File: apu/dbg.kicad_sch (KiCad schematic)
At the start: 12 parts, among them U1 X818336-001, U3 AT25xxx

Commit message: Internal Connectors
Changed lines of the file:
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@@
 	(bus
 		(pts
-			(xy 31.75 71.12) (xy 36.83 71.12)
+			(xy 34.29 71.12) (xy 36.83 71.12)
 		)
 		(stroke
@@
 	(bus
 		(pts
-			(xy 143.51 68.58) (xy 148.59 68.58)
+			(xy 148.59 66.04) (xy 148.59 68.58)
 		)
 		(stroke
@@
 	(bus
 		(pts
-			(xy 125.73 63.5) (xy 130.81 63.5)
-		)
-		(stroke
-			(width 0)
-			(type default)
-		)
-	)
-	(bus
-		(pts
-			(xy 262.89 71.12) (xy 267.97 71.12)
+			(xy 125.73 63.5) (xy 125.73 60.96)
+		)
+		(stroke
+			(width 0)
+			(type default)
+		)
+	)
+	(bus
+		(pts
+			(xy 262.89 71.12) (xy 262.89 68.58)
 		)
 		(stroke
@@
 	(hierarchical_label "{XCGPU_DBG}"
 		(shape bidirectional)
-		(at 31.75 71.12 180)
+		(at 34.29 71.12 180)
 		(effects
 			(font
@@
 	(hierarchical_label "{XCGPU_DBG}"
 		(shape bidirectional)
-		(at 130.81 63.5 0)
+		(at 125.73 60.96 90)
 		(effects
 			(font
@@
 	(hierarchical_label "XCGPU{JTAG}"
 		(shape bidirectional)
-		(at 143.51 68.58 180)
-		(effects
-			(font
-				(size 1.27 1.27)
-			)
-			(justify right)
+		(at 148.59 66.04 90)
+		(effects
+			(font
+				(size 1.27 1.27)
+			)
+			(justify left)
 		)
 	)
 	(hierarchical_label "XCGPU{SPI}"
 		(shape bidirectional)
-		(at 267.97 71.12 0)
-		(effects
-			(font
+		(at 262.89 68.58 90)
+		(effects
+			(font

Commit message: Cleanup & Debug I/O
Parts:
- removed JP4: Jumper_3_Open, TestPoint:TestPoint_2Pads_Pitch5.08mm_Drill1.3mm, symbol Jumper:Jumper_3_Open
- added JP4: Jumper_2_Open, symbol Jumper:Jumper_2_Open
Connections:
- net at R33.2: now also JP4.2 (B)
- net at U1.E3 (<DN>SROM_EN): now also JP4.1 (A)
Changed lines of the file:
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@@
 		)
 	)
-	(wire
-		(pts
-			(xy 220.98 62.23) (xy 223.52 62.23)
-		)
-		(stroke
-			(width 0)
-			(type default)
-		)
-	)
 	(bus
 		(pts
@@
 	(wire
 		(pts
-			(xy 210.82 59.69) (xy 210.82 62.23)
+			(xy 242.57 68.58) (xy 242.57 71.12)
 		)
 		(stroke
@@
 	(wire
 		(pts
-			(xy 229.87 66.04) (xy 229.87 71.12)
-		)
-		(stroke
-			(width 0)
-			(type default)
-		)
-	)
-	(wire
-		(pts
 			(xy 173.99 114.3) (xy 176.53 114.3)
 		)
@@
 	(wire
 		(pts
-			(xy 213.36 62.23) (xy 210.82 62.23)
+			(xy 240.03 71.12) (xy 242.57 71.12)
 		)
 		(stroke
@@
 	)
 	(symbol
-		(lib_id "Device:R")
-		(at 217.17 62.23 90)
-		(unit 1)
-		(exclude_from_sim no)
-		(in_bom yes)
-		(on_board yes)
-		(dnp no)
-		(property "Reference" "R33"
-			(at 214.376 59.944 90)
-			(effects
-				(font
-					(size 1.27 1.27)
-				)
-			)
-		)
-		(property "Value" "100"
-			(at 220.218 59.944 90)
-			(effects
-				(font
-					(size 1.27 1.27)
-				)
-			)
-		)
-		(property "Footprint" ""
-			(at 217.17 64.008 90)
-			(effects
-				(font
-					(size 1.27 1.27)
-				)
-				(hide yes)
-			)
-		)
-		(property "Datasheet" "~"
-			(at 217.17 62.23 0)
-			(effects
-				(font
-					(size 1.27 1.27)
-				)
-				(hide yes)
-			)
-		)
-		(property "Description" "Resistor"
-			(at 217.17 62.23 0)
-			(effects
-				(font
-					(size 1.27 1.27)
-				)
-				(hide yes)
-			)
-		)
-		(pin "2"
-		)
-		(pin "1"
-		)
-		(instances
-			(project "StingBurst"
-				(path "/16640ecb-e4a4-4594-871b-70047bfba6e0/15d9acf0-ed9b-44aa-a266-2c44722c6abb/b46b0d00-cbe3-40e4-97ce-8507deb9af75"
-					(reference "R33")
-					(unit 1)
-				)
-			)
-		)
-	)
-	(symbol
 		(lib_id "power:VDD")
 		(at 204.47 101.6 0)
@@
 	(symbol
 		(lib_id "power:VDD")
-		(at 210.82 59.69 0)
+		(at 242.57 60.96 0)
 		(unit 1)
 		(exclude_from_sim no)
@@
 		(fields_autoplaced yes)
 		(property "Reference" "#PWR087"
-			(at 210.82 63.5 0)
+			(at 242.57 64.77 0)
 			(effects
 				(font
@@
 		)
 		(property "Value" "V_MEM"
-			(at 210.82 54.61 0)
+			(at 242.57 55.88 0)
 			(effects
 				(font
@@
 		)
 		(property "Footprint" ""
-			(at 210.82 59.69 0)
+			(at 242.57 60.96 0)
 			(effects
 				(font
@@
 		)
 		(property "Datasheet" ""
-			(at 210.82 59.69 0)
+			(at 242.57 60.96 0)
 			(effects
 				(font
@@
 		)
 		(property "Description" "Power symbol creates a global label with name \"VDD\""
-			(at 210.82 59.69 0)
+			(at 242.57 60.96 0)
 			(effects
 				(font
@@
 	)
 	(symbol
-		(lib_id "Jumper:Jumper_3_Open")
-		(at 229.87 62.23 0)
-		(unit 1)
-		(exclude_from_sim no)
-		(in_bom no)
-		(on_board yes)
-		(dnp no)
-		(property "Reference" "JP4"
-			(at 229.87 58.42 0)
-			(effects
-				(font
-					(size 1.27 1.27)
-				)
-			)
-		)
-		(property "Value" "Jumper_3_Open"
-			(at 229.87 58.42 0)
-			(effects
-				(font
-					(size 1.27 1.27)
-				)
-				(hide yes)
-			)
-		)
-		(property "Footprint" "TestPoint:TestPoint_2Pads_Pitch5.08mm_Drill1.3mm"
-			(at 229.87 62.23 0)
-			(effects
-				(font
-					(size 1.27 1.27)
-				)
-				(hide yes)
-			)
-		)
-		(property "Datasheet" "~"
-			(at 229.87 62.23 0)
-			(effects
-				(font
-					(size 1.27 1.27)
-				)
-				(hide yes)
-			)
-		)
-		(property "Description" "Jumper, 3-pole, both open"
-			(at 229.87 62.23 0)
-			(effects
-				(font
-					(size 1.27 1.27)
-				)
-				(hide yes)
-			)
-		)
-		(pin "2"
-		)
-		(pin "1"
-		)
-		(pin "3"
-		)
-		(instances
-			(project "StingBurst"
-				(path "/16640ecb-e4a4-4594-871b-70047bfba6e0/15d9acf0-ed9b-44aa-a266-2c44722c6abb/b46b0d00-cbe3-40e4-97ce-8507deb9af75"
-					(reference "JP4")
-					(unit 1)
-				)
-			)
-		)
-	)
-	(symbol
 		(lib_id "power:VDD")
 		(at 234.95 99.06 0)
@@
 	)
 	(symbol
-		(lib_id "power:GND")
-		(at 236.22 62.23 0)
+		(lib_id "Jumper:Jumper_2_Open")
+		(at 234.95 71.12 0)
 		(unit 1)
 		(exclude_from_sim no)
@@
 		(on_board yes)
 		(dnp no)
-		(fields_autoplaced yes)
-		(property "Reference" "#PWR088"
-			(at 236.22 68.58 0)
+		(property "Reference" "JP4"
+			(at 234.95 67.31 0)
+			(effects
+				(font
+					(size 1.27 1.27)
+				)
+			)
+		)
+		(property "Value" "Jumper_2_Open"
+			(at 234.95 67.31 0)
 			(effects
 				(font
@@
 			)
 		)
-		(property "Value" "GND"
-			(at 236.22 67.31 0)
+		(property "Footprint" ""
+			(at 234.95 71.12 0)
+			(effects
+				(font
+					(size 1.27 1.27)
+				)
+				(hide yes)
+			)
+		)
+		(property "Datasheet" "~"
+			(at 234.95 71.12 0)
+			(effects
+				(font
+					(size 1.27 1.27)
+				)
+				(hide yes)
+			)
+		)
+		(property "Description" "Jumper, 2-pole, open"
+			(at 234.95 71.12 0)
+			(effects
+				(font
+					(size 1.27 1.27)
+				)
+				(hide yes)
+			)
+		)
+		(pin "2"
+		)
+		(pin "1"
+		)
+		(instances
+			(project "Mantaray"
+				(path "/16640ecb-e4a4-4594-871b-70047bfba6e0/15d9acf0-ed9b-44aa-a266-2c44722c6abb/b46b0d00-cbe3-40e4-97ce-8507deb9af75"
+					(reference "JP4")
+					(unit 1)
+				)
+			)
+		)
+	)
+	(symbol
+		(lib_id "Device:R")
+		(at 242.57 64.77 0)
+		(unit 1)
+		(exclude_from_sim no)
+		(in_bom yes)
+		(on_board yes)
+		(dnp no)
+		(property "Reference" "R33"
+			(at 244.094 63.5 0)
 			(effects
 				(font
 					(size 1.27 1.27)
 				)
+				(justify left)
+			)
+		)
+		(property "Value" "100"
+			(at 244.094 66.04 0)
+			(effects
+				(font
+					(size 1.27 1.27)
+				)
+				(justify left)
 			)
 		)
 		(property "Footprint" ""
-			(at 236.22 62.23 0)
+			(at 240.792 64.77 90)
 			(effects
 				(font
@@
 			)
 		)
-		(property "Datasheet" ""
-			(at 236.22 62.23 0)
+		(property "Datasheet" "~"
+			(at 242.57 64.77 0)
 			(effects
 				(font
@@
 			)
 		)
-		(property "Description" "Power symbol creates a global label with name \"GND\" , ground"
-			(at 236.22 62.23 0)
+		(property "Description" "Resistor"
+			(at 242.57 64.77 0)
 			(effects
 				(font
@@
 		(pin "1"
 		)
+		(pin "2"
+		)
 		(instances
-			(project "StingBurst"
+			(project "Mantaray"
 				(path "/16640ecb-e4a4-4594-871b-70047bfba6e0/15d9acf0-ed9b-44aa-a266-2c44722c6abb/b46b0d00-cbe3-40e4-97ce-8507deb9af75"
-					(reference "#PWR088")
+					(reference "R33")
 					(unit 1)
 				)

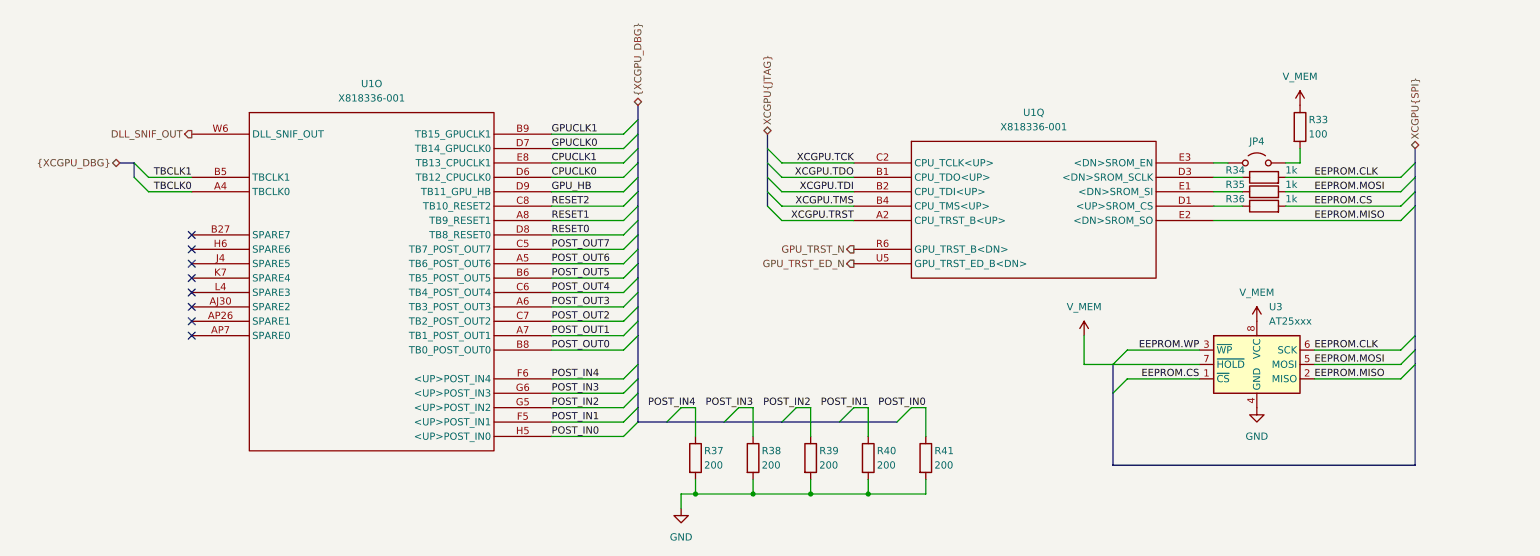
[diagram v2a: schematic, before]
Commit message: Nand Flash, Sata Connectors and removing (hopefully) unnecessary things
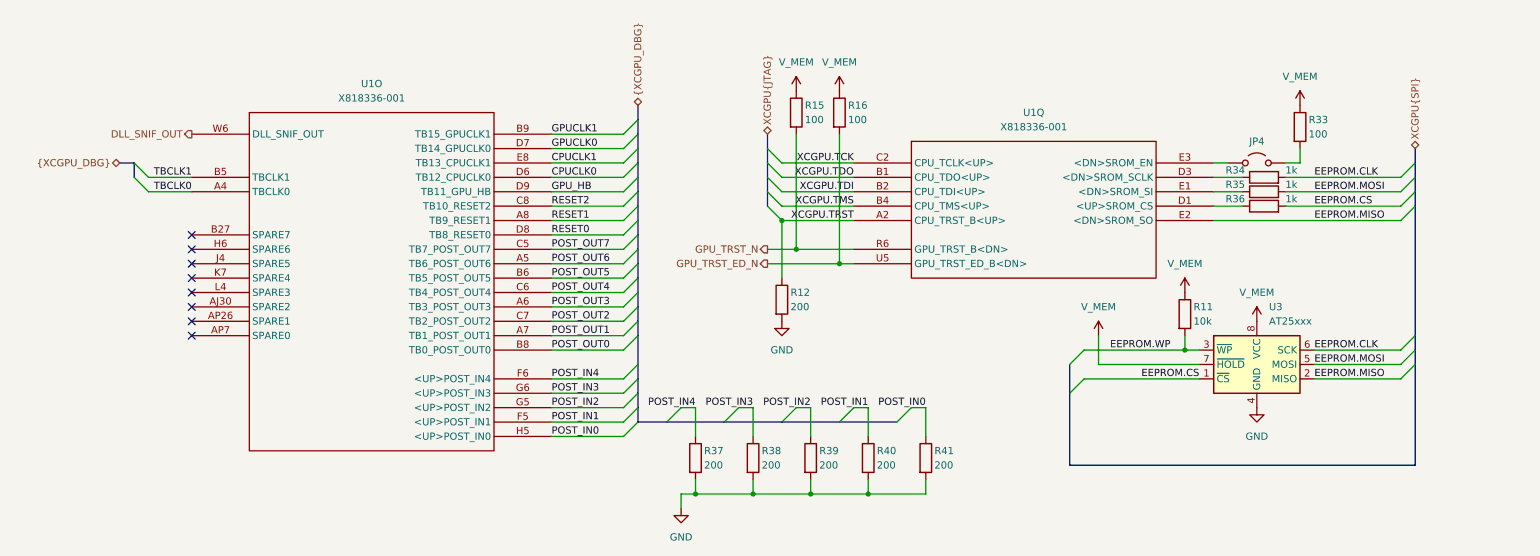
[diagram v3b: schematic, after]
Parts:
- added R11: 10k, symbol Device:R
- added R12: 200, symbol Device:R
- added R15, R16: 100, symbol Device:R
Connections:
- net EEPROM.WP: now also R11.2
- net GND: now also R12.2
- net GPU_TRST_ED_N: now also R16.2
- net GPU_TRST_N: now also R15.2
- net V_MEM: now also R11.1, R15.1, R16.1
- net XCGPU.TRST: now also R12.1

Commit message: Multipurpose and standby power rails, Reannotated schematic
Added V_1P2, V_1P8, V_5P0DUAL, V_EFUSE, V_GPUPCIE, V_3P3STBY and V_1P2STBY
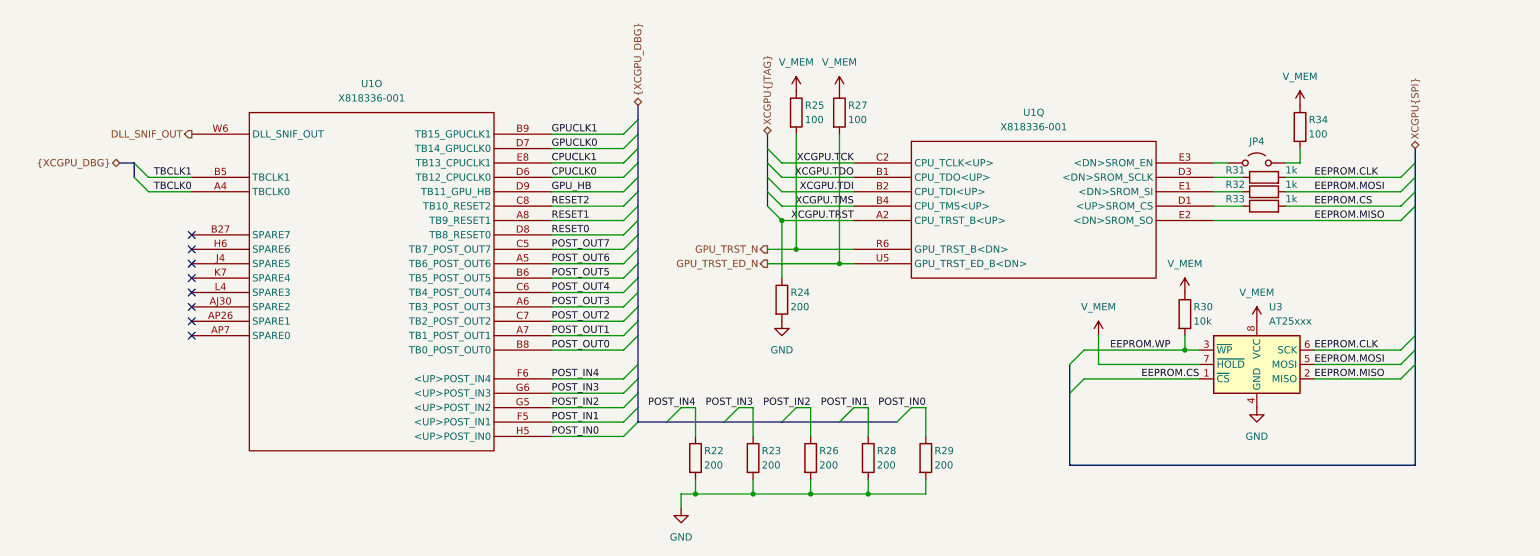
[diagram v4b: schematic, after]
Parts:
- renumbered R37 to R22, R38 to R23, R12 to R24, R15 to R25, R39 to R26, R16 to R27, R40 to R28, R41 to R29, R11 to R30, R34 to R31, R35 to R32, R36 to R33, R33 to R34
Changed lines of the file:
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@@
 		(on_board yes)
 		(dnp no)
-		(property "Reference" "R34"
+		(property "Reference" "R31"
 			(at 231.14 72.39 90)
 			(effects
@@
 			(project "StingBurst"
 				(path "/16640ecb-e4a4-4594-871b-70047bfba6e0/15d9acf0-ed9b-44aa-a266-2c44722c6abb/b46b0d00-cbe3-40e4-97ce-8507deb9af75"
-					(reference "R34")
+					(reference "R31")
 					(unit 1)
 				)
@@
 		(dnp no)
 		(fields_autoplaced yes)
-		(property "Reference" "#PWR014"
+		(property "Reference" "#PWR081"
 			(at 222.25 97.79 0)
 			(effects
@@
 			(project "Mantaray"
 				(path "/16640ecb-e4a4-4594-871b-70047bfba6e0/15d9acf0-ed9b-44aa-a266-2c44722c6abb/b46b0d00-cbe3-40e4-97ce-8507deb9af75"
-					(reference "#PWR014")
+					(reference "#PWR081")
 					(unit 1)
 				)
@@
 		(dnp no)
 		(fields_autoplaced yes)
-		(property "Reference" "#PWR090"
+		(property "Reference" "#PWR080"
 			(at 207.01 105.41 0)
 			(effects
@@
 			(project "StingBurst"
 				(path "/16640ecb-e4a4-4594-871b-70047bfba6e0/15d9acf0-ed9b-44aa-a266-2c44722c6abb/b46b0d00-cbe3-40e4-97ce-8507deb9af75"
-					(reference "#PWR090")
+					(reference "#PWR080")
 					(unit 1)
 				)
@@
 		(on_board yes)
 		(dnp no)
-		(property "Reference" "R39"
+		(property "Reference" "R26"
 			(at 157.734 121.92 0)
 			(effects
@@
 			(project "StingBurst"
 				(path "/16640ecb-e4a4-4594-871b-70047bfba6e0/15d9acf0-ed9b-44aa-a266-2c44722c6abb/b46b0d00-cbe3-40e4-97ce-8507deb9af75"
-					(reference "R39")
+					(reference "R26")
 					(unit 1)
 				)
@@
 		(on_board yes)
 		(dnp no)
-		(property "Reference" "R36"
+		(property "Reference" "R33"
 			(at 231.14 77.47 90)
 			(effects
@@
 			(project "StingBurst"
 				(path "/16640ecb-e4a4-4594-871b-70047bfba6e0/15d9acf0-ed9b-44aa-a266-2c44722c6abb/b46b0d00-cbe3-40e4-97ce-8507deb9af75"
-					(reference "R36")
+					(reference "R33")
 					(unit 1)
 				)
@@
 		(dnp no)
 		(fields_autoplaced yes)
-		(property "Reference" "#PWR019"
+		(property "Reference" "#PWR078"
 			(at 153.67 62.23 0)
 			(effects
@@
 			(project "Mantaray"
 				(path "/16640ecb-e4a4-4594-871b-70047bfba6e0/15d9acf0-ed9b-44aa-a266-2c44722c6abb/b46b0d00-cbe3-40e4-97ce-8507deb9af75"
-					(reference "#PWR019")
+					(reference "#PWR078")
 					(unit 1)
 				)
@@
 		(on_board yes)
 		(dnp no)
-		(property "Reference" "R38"
+		(property "Reference" "R23"
 			(at 147.574 121.92 0)
 			(effects
@@
 			(project "StingBurst"
 				(path "/16640ecb-e4a4-4594-871b-70047bfba6e0/15d9acf0-ed9b-44aa-a266-2c44722c6abb/b46b0d00-cbe3-40e4-97ce-8507deb9af75"
-					(reference "R38")
+					(reference "R23")
 					(unit 1)
 				)
@@
 		(on_board yes)
 		(dnp no)
-		(property "Reference" "R40"
+		(property "Reference" "R28"
 			(at 167.894 121.92 0)
 			(effects
@@
 			(project "StingBurst"
 				(path "/16640ecb-e4a4-4594-871b-70047bfba6e0/15d9acf0-ed9b-44aa-a266-2c44722c6abb/b46b0d00-cbe3-40e4-97ce-8507deb9af75"
-					(reference "R40")
+					(reference "R28")
 					(unit 1)
 				)
@@
 		(on_board yes)
 		(dnp no)
-		(property "Reference" "R37"
+		(property "Reference" "R22"
 			(at 137.414 121.92 0)
 			(effects
@@
 			(project "StingBurst"
 				(path "/16640ecb-e4a4-4594-871b-70047bfba6e0/15d9acf0-ed9b-44aa-a266-2c44722c6abb/b46b0d00-cbe3-40e4-97ce-8507deb9af75"
-					(reference "R37")
+					(reference "R22")
 					(unit 1)
 				)
@@
 		(dnp no)
 		(fields_autoplaced yes)
-		(property "Reference" "#PWR087"
+		(property "Reference" "#PWR084"
 			(at 242.57 64.77 0)
 			(effects
@@
 			(project "StingBurst"
 				(path "/16640ecb-e4a4-4594-871b-70047bfba6e0/15d9acf0-ed9b-44aa-a266-2c44722c6abb/b46b0d00-cbe3-40e4-97ce-8507deb9af75"
-					(reference "#PWR087")
+					(reference "#PWR084")
 					(unit 1)
 				)
@@
 		(dnp no)
 		(fields_autoplaced yes)
-		(property "Reference" "#PWR089"
+		(property "Reference" "#PWR082"
 			(at 234.95 102.87 0)
 			(effects
@@
 			(project "StingBurst"
 				(path "/16640ecb-e4a4-4594-871b-70047bfba6e0/15d9acf0-ed9b-44aa-a266-2c44722c6abb/b46b0d00-cbe3-40e4-97ce-8507deb9af75"
-					(reference "#PWR089")
+					(reference "#PWR082")
 					(unit 1)
 				)
@@
 		(dnp no)
 		(fields_autoplaced yes)
-		(property "Reference" "#PWR091"
+		(property "Reference" "#PWR083"
 			(at 234.95 120.65 0)
 			(effects
@@
 			(project "StingBurst"
 				(path "/16640ecb-e4a4-4594-871b-70047bfba6e0/15d9acf0-ed9b-44aa-a266-2c44722c6abb/b46b0d00-cbe3-40e4-97ce-8507deb9af75"
-					(reference "#PWR091")
+					(reference "#PWR083")
 					(unit 1)
 				)
@@
 		(on_board yes)
 		(dnp no)
-		(property "Reference" "R15"
+		(property "Reference" "R25"
 			(at 155.194 60.96 0)
 			(effects
@@
 			(project "Mantaray"
 				(path "/16640ecb-e4a4-4594-871b-70047bfba6e0/15d9acf0-ed9b-44aa-a266-2c44722c6abb/b46b0d00-cbe3-40e4-97ce-8507deb9af75"
-					(reference "R15")
+					(reference "R25")
 					(unit 1)
 				)
@@
 		(dnp no)
 		(fields_autoplaced yes)
-		(property "Reference" "#PWR020"
+		(property "Reference" "#PWR079"
 			(at 161.29 62.23 0)
 			(effects
@@
 			(project "Mantaray"
 				(path "/16640ecb-e4a4-4594-871b-70047bfba6e0/15d9acf0-ed9b-44aa-a266-2c44722c6abb/b46b0d00-cbe3-40e4-97ce-8507deb9af75"
-					(reference "#PWR020")
+					(reference "#PWR079")
 					(unit 1)
 				)
@@
 		(on_board yes)
 		(dnp no)
-		(property "Reference" "R11"
+		(property "Reference" "R30"
 			(at 223.774 96.52 0)
 			(effects
@@
 			(project "Mantaray"
 				(path "/16640ecb-e4a4-4594-871b-70047bfba6e0/15d9acf0-ed9b-44aa-a266-2c44722c6abb/b46b0d00-cbe3-40e4-97ce-8507deb9af75"
-					(reference "R11")
+					(reference "R30")
 					(unit 1)
 				)
@@
 		(dnp no)
 		(fields_autoplaced yes)
-		(property "Reference" "#PWR018"
+		(property "Reference" "#PWR077"
 			(at 151.13 105.41 0)
 			(effects
@@
 			(project ""
 				(path "/16640ecb-e4a4-4594-871b-70047bfba6e0/15d9acf0-ed9b-44aa-a266-2c44722c6abb/b46b0d00-cbe3-40e4-97ce-8507deb9af75"
-					(reference "#PWR018")
+					(reference "#PWR077")
 					(unit 1)
 				)
@@
 		(on_board yes)
 		(dnp no)
-		(property "Reference" "R33"
+		(property "Reference" "R34"
 			(at 244.094 63.5 0)
 			(effects
@@
 			(project "Mantaray"
 				(path "/16640ecb-e4a4-4594-871b-70047bfba6e0/15d9acf0-ed9b-44aa-a266-2c44722c6abb/b46b0d00-cbe3-40e4-97ce-8507deb9af75"
-					(reference "R33")
+					(reference "R34")
 					(unit 1)
 				)
@@
 		(on_board yes)
 		(dnp no)
-		(property "Reference" "R12"
+		(property "Reference" "R24"
 			(at 152.654 93.98 0)
 			(effects
@@
 			(project "Mantaray"
 				(path "/16640ecb-e4a4-4594-871b-70047bfba6e0/15d9acf0-ed9b-44aa-a266-2c44722c6abb/b46b0d00-cbe3-40e4-97ce-8507deb9af75"
-					(reference "R12")
+					(reference "R24")
 					(unit 1)
 				)
@@
 		(dnp no)
 		(fields_autoplaced yes)
-		(property "Reference" "#PWR092"
+		(property "Reference" "#PWR076"
 			(at 133.35 138.43 0)
 			(effects
@@
 			(project ""
 				(path "/16640ecb-e4a4-4594-871b-70047bfba6e0/15d9acf0-ed9b-44aa-a266-2c44722c6abb/b46b0d00-cbe3-40e4-97ce-8507deb9af75"
-					(reference "#PWR092")
+					(reference "#PWR076")
 					(unit 1)
 				)
@@
 		(on_board yes)
 		(dnp no)
-		(property "Reference" "R16"
+		(property "Reference" "R27"
 			(at 162.814 60.96 0)
 			(effects
@@
 			(project "Mantaray"
 				(path "/16640ecb-e4a4-4594-871b-70047bfba6e0/15d9acf0-ed9b-44aa-a266-2c44722c6abb/b46b0d00-cbe3-40e4-97ce-8507deb9af75"
-					(reference "R16")
+					(reference "R27")
 					(unit 1)
 				)
@@
 		(on_board yes)
 		(dnp no)
-		(property "Reference" "R41"
+		(property "Reference" "R29"
 			(at 178.054 121.92 0)
 			(effects
@@
 			(project "StingBurst"
 				(path "/16640ecb-e4a4-4594-871b-70047bfba6e0/15d9acf0-ed9b-44aa-a266-2c44722c6abb/b46b0d00-cbe3-40e4-97ce-8507deb9af75"
-					(reference "R41")
+					(reference "R29")
 					(unit 1)
 				)
@@
 		(on_board yes)
 		(dnp no)
-		(property "Reference" "R35"
+		(property "Reference" "R32"
 			(at 231.14 74.93 90)
 			(effects
@@
 			(project "StingBurst"
 				(path "/16640ecb-e4a4-4594-871b-70047bfba6e0/15d9acf0-ed9b-44aa-a266-2c44722c6abb/b46b0d00-cbe3-40e4-97ce-8507deb9af75"
-					(reference "R35")
+					(reference "R32")
 					(unit 1)
 				)
